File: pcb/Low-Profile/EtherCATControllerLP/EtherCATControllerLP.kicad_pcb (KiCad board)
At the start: 2 copper layers, 52 x 52 mm, 0 parts

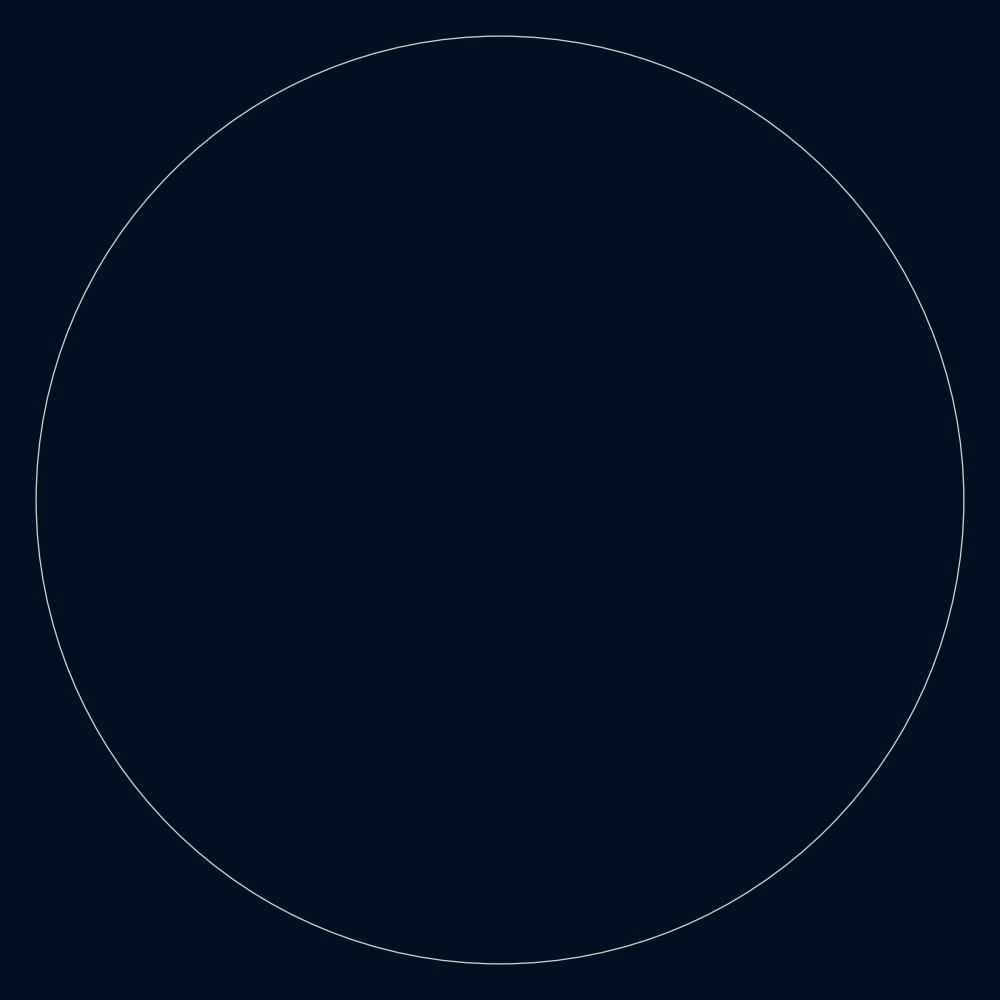
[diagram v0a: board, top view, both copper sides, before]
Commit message: Added Ethernet PHY
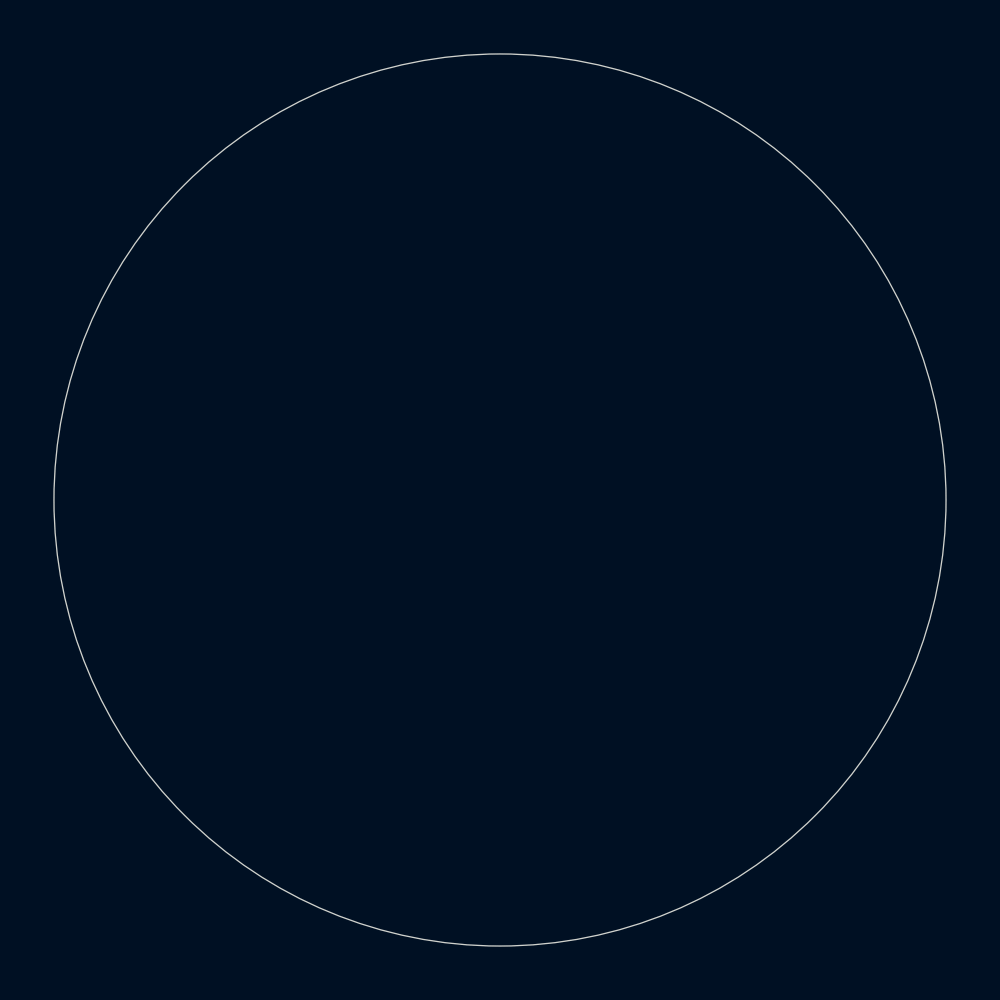
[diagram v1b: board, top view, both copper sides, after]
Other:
- board size 52 x 52 mm -> 50 x 50 mm
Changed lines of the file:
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@@
 	(gr_circle
 		(center 150 100)
-		(end 176 100)
+		(end 175 100)
 		(stroke
 			(width 0.05)
